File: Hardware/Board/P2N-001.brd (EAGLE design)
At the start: 72 x 72 mm, 40 parts, among them IC1 4053N, IC2 LTC485N, IC3 74LS07N, IC4 LTC485N, K1 G5V1, T1 2SC1815, X1 HIROSE-DX10LM1-14SE

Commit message: Cleaned up board design.
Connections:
- net TXRETURNII renamed TX2RETURN
- net TXSENDZV renamed TX2SEND
- removed net SENS0: MC1.P$3
- removed net SENS1: MC1.P$4
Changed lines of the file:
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@@
 <via x="22.6314" y="32.4612" extent="1-16" drill="0.6096"/>
 </signal>
-<signal name="TXRETURNII">
+<signal name="TX2RETURN">
 <contactref element="R12" pad="2"/>
 <contactref element="SV1" pad="5"/>
@@
 <via x="54.6354" y="5.9436" extent="1-16" drill="0.6096"/>
 </signal>
-<signal name="TXSENDZV">
+<signal name="TX2SEND">
 <contactref element="R10" pad="2"/>
 <contactref element="SV1" pad="4"/>
@@
 <wire x1="39.5478" y1="64.6938" x2="39.37" y2="64.77" width="0.254" layer="16"/>
 </signal>
-<signal name="SENS0">
-<contactref element="MC1" pad="P$3"/>
-</signal>
-<signal name="SENS1">
-<contactref element="MC1" pad="P$4"/>
-</signal>
 <signal name="RXSEND">

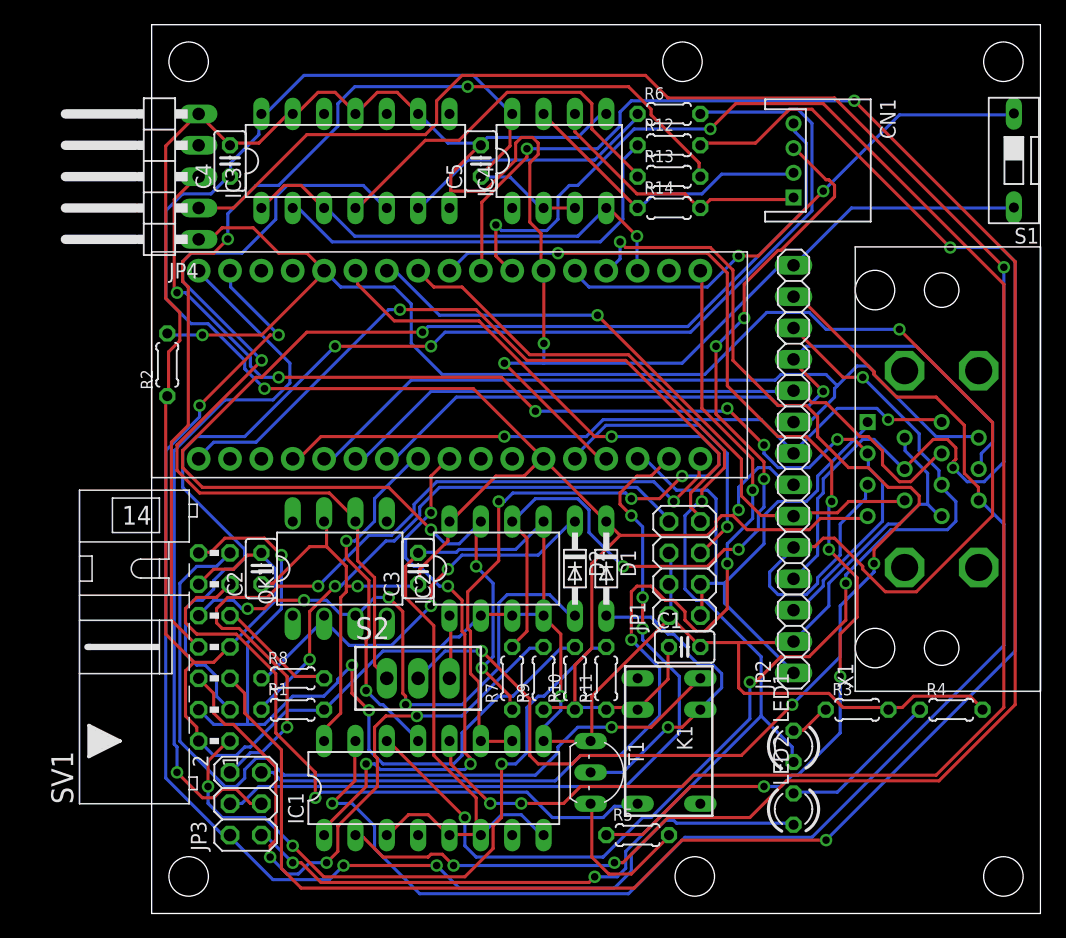
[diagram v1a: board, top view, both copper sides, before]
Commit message: Changed USB connector from Pinheader to Micro-B.
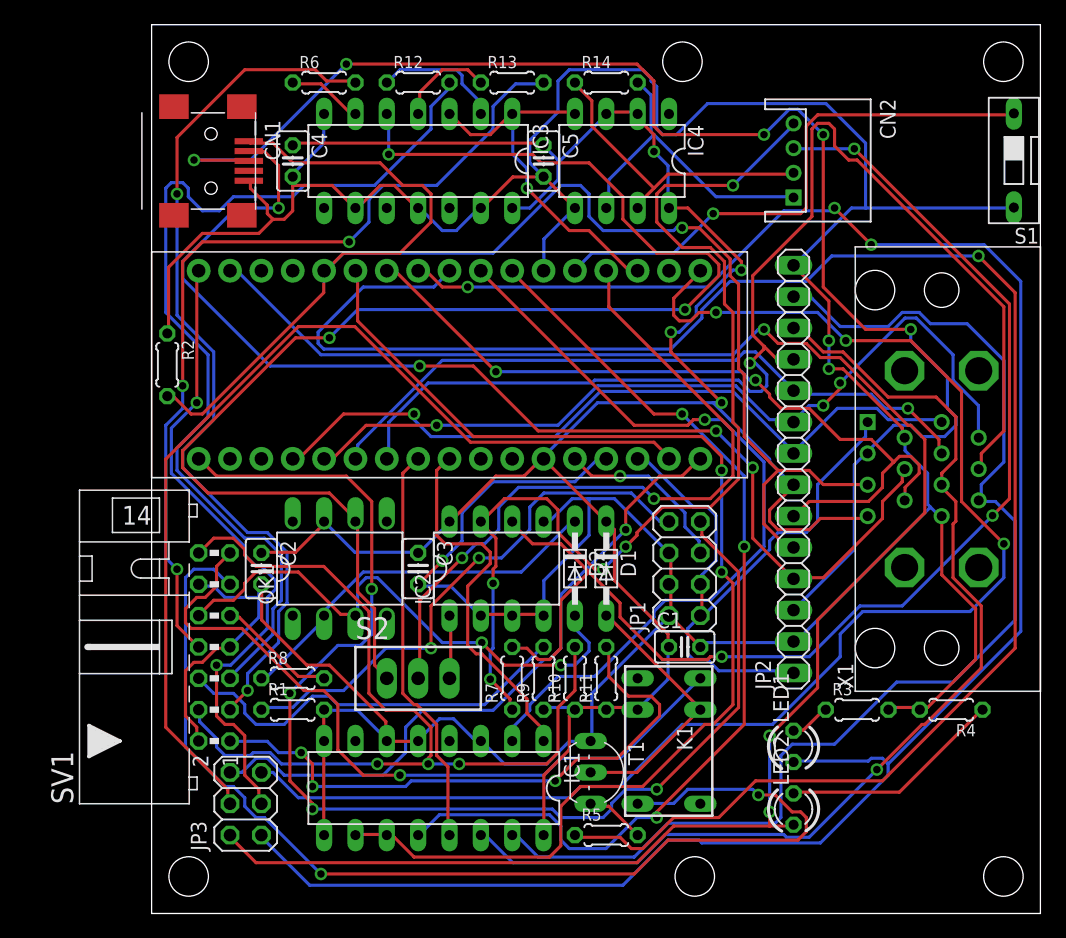
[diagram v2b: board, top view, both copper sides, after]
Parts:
- removed JP4: (no value), pinhead:1X05/90
- added CN2: (no value), jst-ph:S4B-PH-K-S
- CN1: device jst-ph:S4B-PH-K-S -> adafruit:USB-MINIB
- moved CN1 48.2 mm to (3.81, 61.0)
- moved R6 28.1 mm to (14.0, 67.3)
- moved R12 20.9 mm to (21.6, 67.3)
- moved R13 14.8 mm to (29.2, 67.3)
- moved R14 11.4 mm to (36.8, 67.3)
- moved C4 5.08 mm to (11.4, 61.0), turned to 270 degrees
- moved C5 5.08 mm to (31.8, 61.0), turned to 270 degrees
- moved IC3 5.08 mm to (21.6, 61.0), turned to 180 degrees
- moved IC4 5.08 mm to (38.1, 61.0), turned to 180 degrees
- moved R5 2.54 mm to (36.8, 6.35)
- turned C2 to 270 degrees
- turned C3 to 270 degrees
- turned IC1 to 180 degrees
- turned R2 to 270 degrees
- turned R4 to 180 degrees
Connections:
- net GND: now also CN1.GND; no longer JP4.5
- net PD: now also CN1.VBUS; no longer JP4.1
- net RX+: now also CN2.3; no longer CN1.3
- net RX-: now also CN2.4; no longer CN1.4
- net TX+: now also CN2.1; no longer CN1.1
- net TX-: now also CN2.2; no longer CN1.2
- net USBD+: now also CN1.D+; no longer JP4.3
- net USBD-: now also CN1.D-; no longer JP4.2
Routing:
- net SCL: track 154.6 -> 64.7 mm, vias 4 -> 1
- net TX2RETURN: track 148.6 -> 78.5 mm, vias 2 -> 0
- net SDA: track 142.6 -> 79.2 mm, vias 4 -> 3
- net RELAY: track 89.8 -> 146.8 mm, vias 5 -> 1
- net GPIO0: track 110.2 -> 163.3 mm
- net RX: track 101.7 -> 58.6 mm, vias 4 -> 2
- net MIDIRX: track 73.6 -> 116.4 mm, vias 1 -> 3
- net GPIO1: track 105.7 -> 148.1 mm, vias 4 -> 3
- net LED: track 58.9 -> 100.0 mm, vias 1 -> 4
- net GND: track 394.4 -> 355.9 mm
- net ZVA: track 53.7 -> 90.7 mm, vias 1 -> 2
- net ANLG3: track 65.3 -> 99.7 mm
- net RXRETURN: track 103.5 -> 72.2 mm
- net MOSI: track 86.3 -> 116.9 mm
- net USBD-: track 123.4 -> 94.2 mm, vias 2 -> 4
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
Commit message: Changed USB con to Sunhayatos connector board. Changed USB connector to Sunhayato's connector board. Also removed ZeroVoltage function.
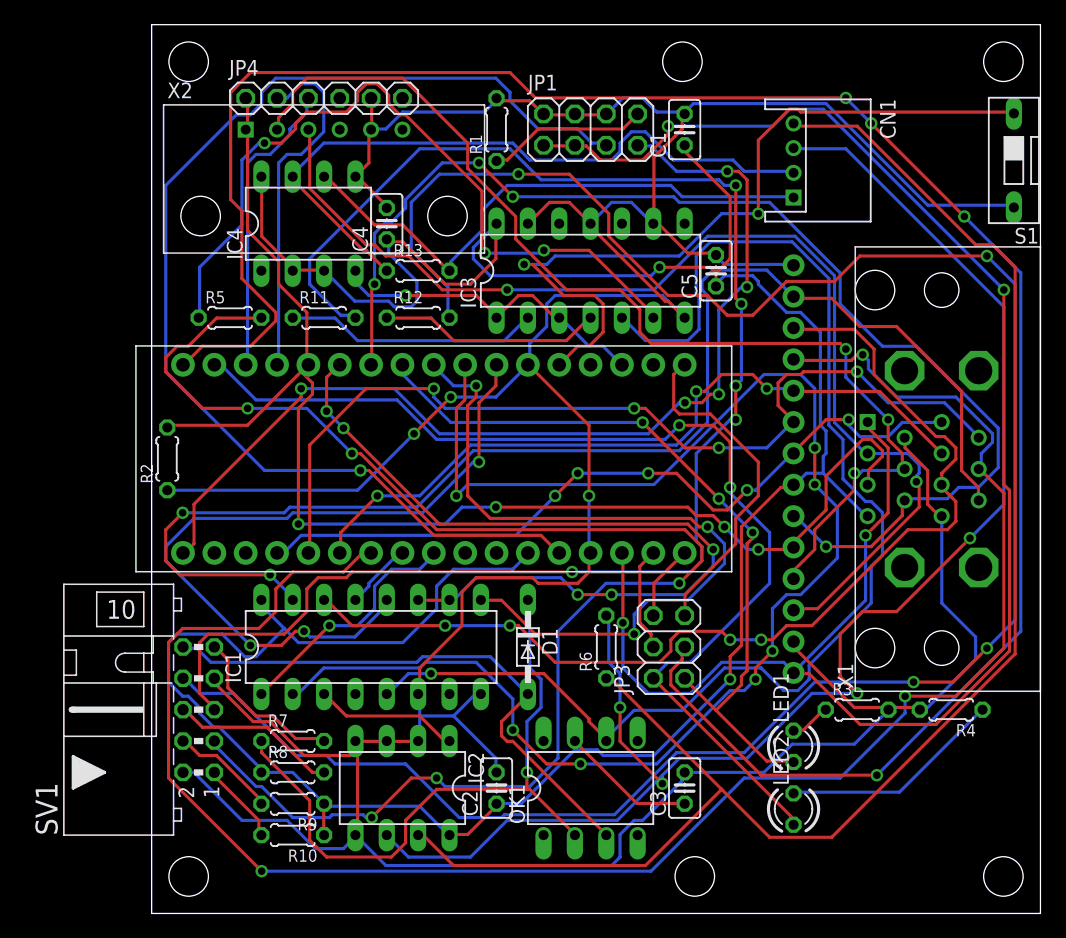
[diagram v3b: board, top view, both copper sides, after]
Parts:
- removed CN2: (no value), jst-ph:S4B-PH-K-S
- removed D2: BAS15, diode:DO34-7
- removed K1: G5V1, relay:G5V1
- removed R14: 120, resistor:0204/5
- removed S2: TL36PO, switch:TL3XPO
- removed T1: 2SC1815, transistor:TO92-ECB
- added JP4: (no value), adafruit:1X06
- added X2: SUNHAYATO-USB-CK37, con-sunhayato-usb:SUNHAYATO-USB-CK37
- CN1: device adafruit:USB-MINIB -> jst-ph:S4B-PH-K-S
- JP2: device pinhead:1X14 -> adafruit:1X14-CB
- R13, R6: value 220 -> 120
- R5: value 3.3k -> 220
- R7: value 120 -> 220
- SV1: device con-ml:ML14L -> con-ml:ML10L
- moved R5 51.8 mm to (6.35, 48.3)
- moved R6 51.1 mm to (36.8, 21.6), turned to 90 degrees
- moved R1 49.8 mm to (27.9, 63.5), turned to 90 degrees
- moved CN1 48.2 mm to (52.0, 61.0)
- moved C1 41.9 mm to (43.2, 63.5), turned to 90 degrees
- moved R11 37.1 mm to (14.0, 48.3), turned to 0 degrees
- moved JP3 36.6 mm to (41.9, 21.6)
- moved JP1 36.4 mm to (35.6, 63.5), turned to 0 degrees
- moved C3 28.0 mm to (43.2, 10.2), turned to 90 degrees
- moved OK1 27.0 mm to (35.6, 10.2)
- moved R10 26.2 mm to (11.4, 6.35), turned to 180 degrees
- moved C2 26.1 mm to (27.9, 10.2), turned to 90 degrees
- moved IC4 25.9 mm to (12.7, 55.9), turned to 0 degrees
- moved R9 22.7 mm to (11.4, 8.89), turned to 180 degrees
- moved IC2 19.3 mm to (20.3, 10.2), turned to 180 degrees
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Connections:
- removed net RELAY: MC1.P$9, R5.1
- removed net ZVA: K1.5, SV1.11
- removed net ZVB: K1.10, SV1.13
- new net N$5: JP4.2, MC1.P$4
- net GND: now also JP4.5, X2.P$5; no longer CN1.GND, IC1.3, IC1.5, IC1.9, SV1.12, T1.E
- net MIDIRX: now also IC1.5; no longer S2.1
- net N$15: now also D1.C, R7.1; no longer D2.C, R8.1
- net N$2: now also R11.1; no longer R12.1
- net N$3: now also R5.1; no longer R6.1
- net N$4: now also R12.1; no longer R13.1
- net N$6: now also JP4.3, MC1.P$3; no longer D1.A, K1.9, T1.C
- net N$8: now also IC1.9, MC1.P$9; no longer R5.2, T1.B
- net PD: now also JP4.1, X2.P$1; no longer CN1.VBUS
- net RX: no longer S2.2
- net RX+: now also CN1.3, R6.2; no longer CN2.3, R7.2
- net RX-: now also CN1.4, R6.1; no longer CN2.4, R7.1
- net RXA: now also R7.2; no longer R8.2
- net RXK: now also D1.A; no longer D2.A
- net RXRETURN: now also R5.2; no longer R6.2
- net RXSEND: now also R10.2; no longer R11.2
- net TX+: now also CN1.1, R13.2; no longer CN2.1, R14.2
- net TX-: now also CN1.2, R13.1; no longer CN2.2, R14.1
- net TX2RETURN: now also R11.2; no longer R12.2
- net TX2SEND: now also R9.2; no longer R10.2, SV1.14
- net TXRETURN: now also R12.2; no longer R13.2
- net TXSEND: now also R8.2; no longer R9.2
- net USBD+: now also X2.P$3; no longer CN1.D+
- net USBD-: now also X2.P$2; no longer CN1.D-
- net VCC: now also R8.1; no longer D1.C, K1.2, R11.1
- net XMIDIRX: now also IC1.3; no longer S2.3
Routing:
- net RELAY: track 146.8 -> 0.00 mm, vias 1 -> 0
- net GPIO2: track 52.5 -> 169.2 mm, vias 2 -> 4
- net TXRETURN: track 70.3 -> 175.1 mm, vias 3 -> 4
- net GPIO0: track 163.3 -> 61.7 mm
- net VDD: track 52.7 -> 146.8 mm, vias 0 -> 4
- net ZVA: track 90.7 -> 0.00 mm, vias 2 -> 0
- net MOSI: track 116.9 -> 27.5 mm, vias 3 -> 0
- net RST: track 14.5 -> 95.6 mm
- net MISO: track 79.9 -> 8.54 mm
- net TX2SEND: track 74.4 -> 8.70 mm, vias 3 -> 0
- net GPIO1: track 148.1 -> 87.3 mm, vias 3 -> 2
- net ZVB: track 59.8 -> 0.00 mm, vias 1 -> 0
- net VCC: track 181.2 -> 240.2 mm, vias 4 -> 2
- net RX: track 58.6 -> 0.00 mm, vias 2 -> 0
- net N$8: track 4.90 -> 61.6 mm, vias 0 -> 3
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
